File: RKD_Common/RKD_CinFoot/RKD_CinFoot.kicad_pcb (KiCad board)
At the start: 2 copper layers, 81 x 11.9 mm, 5 parts

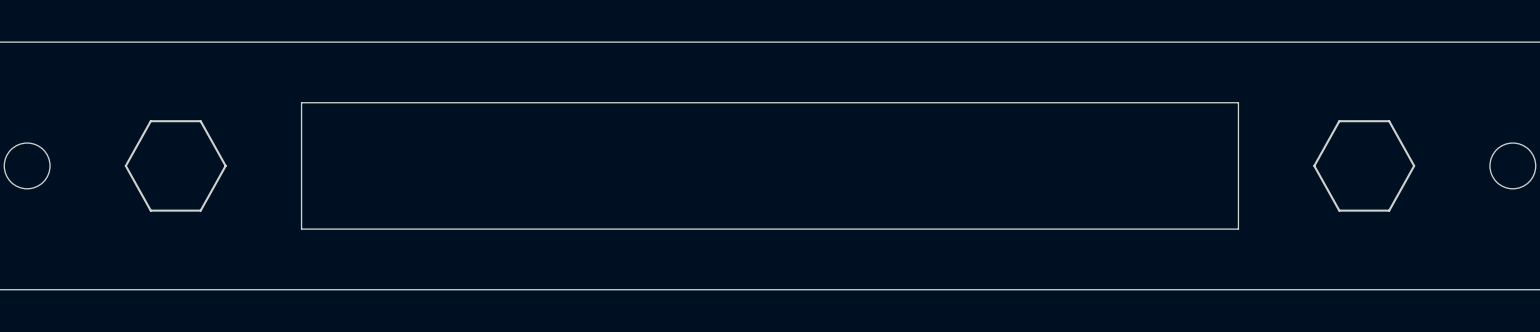
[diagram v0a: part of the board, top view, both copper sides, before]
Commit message: 部品誤り修正
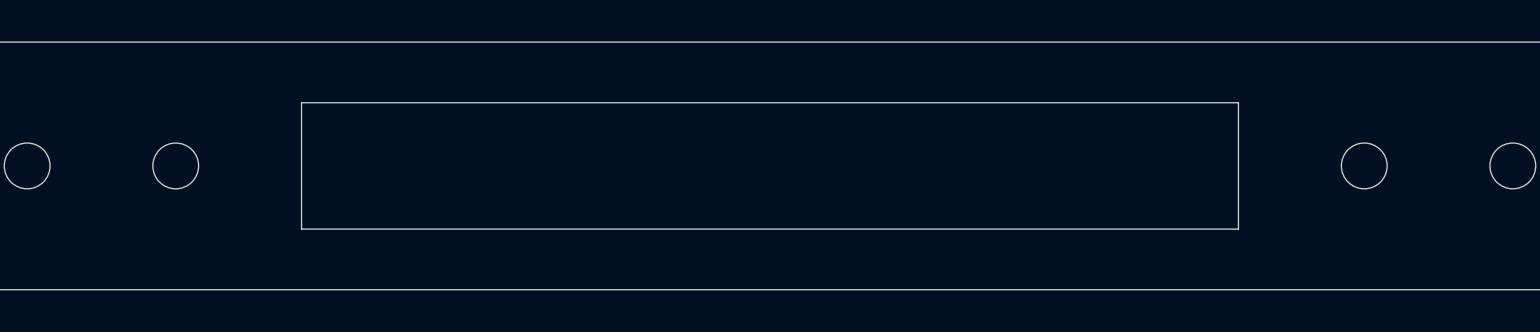
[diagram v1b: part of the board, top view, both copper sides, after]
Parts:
- Ref** (x2): footprint kbd_Hole:m2_Spacer_Hole_hex -> kbd_Hole:m2_Screw_Hole
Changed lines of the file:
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@@
 		)
 	)
-	(footprint "kbd_Hole:m2_Spacer_Hole_hex"
+	(footprint "kbd_Hole:m2_Screw_Hole"
 		(layer "F.Cu")
 		(at 121.44375 51.196875)
@@
 			)
 		)
-		(property "Footprint" "kbd_Hole:m2_Spacer_Hole_hex"
+		(property "Footprint" "kbd_Hole:m2_Screw_Hole"
 			(at 0 0 0)
 			(layer "F.Fab")
@@
 		)
 		(attr exclude_from_pos_files exclude_from_bom)
-		(fp_line
-			(start -2.4 0)
-			(end -1.2 2.15)
+		(fp_circle
+			(center 0 0)
+			(end 2.2 0)
 			(stroke
-				(width 0.1)
+				(width 0.15)
 				(type solid)
 			)
-			(layer "Edge.Cuts")
+			(fill none)
+			(layer "Cmts.User")
 		)
-		(fp_line
-			(start -1.2 -2.15)
-			(end -2.4 0)
+		(fp_circle
+			(center 0 0)
+			(end 2.45 0)
 			(stroke
-				(width 0.1)
+				(width 0.05)
 				(type solid)
 			)
-			(layer "Edge.Cuts")
+			(fill none)
+			(layer "F.CrtYd")
 		)
-		(fp_line
-			(start -1.2 2.15)
-			(end 1.2 2.15)
-			(stroke
-				(width 0.1)
-				(type solid)
+		(fp_text user "${REFERENCE}"
+			(at 0.3 0 0)
+			(layer "F.Fab")
+			(effects
+				(font
+					(size 1 1)
+					(thickness 0.15)
+				)
 			)
-			(layer "Edge.Cuts")
 		)
-		(fp_line
-			(start 1.2 -2.15)
-			(end -1.2 -2.15)
-			(stroke
-				(width 0.1)
-				(type solid)
-			)
-			(layer "Edge.Cuts")
-		)
-		(fp_line
-			(start 1.2 2.15)
-			(end 2.4 0)
-			(stroke
-				(width 0.1)
-				(type solid)
-			)
-			(layer "Edge.Cuts")
-		)
-		(fp_line
-			(start 2.4 0)
-			(end 1.2 -2.15)
-			(stroke
-				(width 0.1)
-				(type solid)
-			)
-			(layer "Edge.Cuts")
+		(pad "" np_thru_hole circle
+			(at 0 0)
+			(size 2.2 2.2)
+			(drill 2.2)
+			(layers "*.Cu" "*.Mask")
 		)
 	)
-	(footprint "kbd_Hole:m2_Spacer_Hole_hex"
+	(footprint "kbd_Hole:m2_Screw_Hole"
 		(layer "F.Cu")
 		(at 64.29375 51.196875)
@@
 			)
 		)
-		(property "Footprint" "kbd_Hole:m2_Spacer_Hole_hex"
+		(property "Footprint" "kbd_Hole:m2_Screw_Hole"
 			(at 0 0 0)
 			(layer "F.Fab")
@@
 		)
 		(attr exclude_from_pos_files exclude_from_bom)
-		(fp_line
-			(start -2.4 0)
-			(end -1.2 2.15)
+		(fp_circle
+			(center 0 0)
+			(end 2.2 0)
 			(stroke
-				(width 0.1)
+				(width 0.15)
 				(type solid)
 			)
-			(layer "Edge.Cuts")
+			(fill none)
+			(layer "Cmts.User")
 		)
-		(fp_line
-			(start -1.2 -2.15)
-			(end -2.4 0)
+		(fp_circle
+			(center 0 0)
+			(end 2.45 0)
 			(stroke
-				(width 0.1)
+				(width 0.05)
 				(type solid)
 			)
-			(layer "Edge.Cuts")
+			(fill none)
+			(layer "F.CrtYd")
 		)
-		(fp_line
-			(start -1.2 2.15)
-			(end 1.2 2.15)
-			(stroke
-				(width 0.1)
-				(type solid)
+		(fp_text user "${REFERENCE}"
+			(at 0.3 0 0)
+			(layer "F.Fab")
+			(effects
+				(font
+					(size 1 1)
+					(thickness 0.15)
+				)
 			)
-			(layer "Edge.Cuts")
 		)
-		(fp_line
-			(start 1.2 -2.15)
-			(end -1.2 -2.15)
-			(stroke
-				(width 0.1)
-				(type solid)
-			)
-			(layer "Edge.Cuts")
-		)
-		(fp_line
-			(start 1.2 2.15)
-			(end 2.4 0)
-			(stroke
-				(width 0.1)
-				(type solid)
-			)
-			(layer "Edge.Cuts")
-		)
-		(fp_line
-			(start 2.4 0)
-			(end 1.2 -2.15)
-			(stroke
-				(width 0.1)
-				(type solid)
-			)
-			(layer "Edge.Cuts")
+		(pad "" np_thru_hole circle
+			(at 0 0)
+			(size 2.2 2.2)
+			(drill 2.2)
+			(layers "*.Cu" "*.Mask")
 		)
 	)

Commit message: Common UpdateFootPrint
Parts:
- removed the Ref** at (128.6, 51.2)
- removed the Ref** at (121.4, 51.2)
- removed the Ref** at (64.3, 51.2)
- removed the Ref** at (57.1, 51.2)
- added Ref**: Val**, kbd_Hole:m2_Screw_Hole, F.Cu at (123.2, 67.0)
- added Ref**: Val**, kbd_Hole:m2_Screw_Hole, F.Cu at (58.9, 67.0)
- added Ref**: Val**, kbd_Hole:m2_Screw_Hole, F.Cu at (66.1, 67.0)
- added Ref**: Val**, kbd_Hole:m2_Screw_Hole, F.Cu at (130.4, 67.0)
- moved LED3 15.9 mm to (94.7, 67.0)
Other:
- board size 81 x 11.9 mm -> 76.2 x 11.9 mm
- board text added: "RKD_CinderellaFoot v1.0"
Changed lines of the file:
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@@
 	(footprint "kbd_Hole:m2_Screw_Hole"
 		(layer "F.Cu")
-		(at 128.5875 51.196875)
+		(at 123.229892 66.972702)
 		(descr "Mounting Hole 2.2mm, no annular, M2")
 		(tags "mounting hole 2.2mm no annular m2")
@@
 	(footprint "kbd_Hole:m2_Screw_Hole"
 		(layer "F.Cu")
-		(at 121.44375 51.196875)
+		(at 58.936142 66.972702)
 		(descr "Mounting Hole 2.2mm, no annular, M2")
 		(tags "mounting hole 2.2mm no annular m2")
@@
 	(footprint "kbd_Hole:m2_Screw_Hole"
 		(layer "F.Cu")
-		(at 64.29375 51.196875)
+		(at 66.079892 66.972702)
 		(descr "Mounting Hole 2.2mm, no annular, M2")
 		(tags "mounting hole 2.2mm no annular m2")
@@
 		)
 	)
+	(footprint "Rikkodo_FootPrint:rkd_KeyHall_6wx45_Cinderella"
+		(layer "F.Cu")
+		(at 94.654952 66.972702)
+		(property "Reference" "LED3"
+			(at 6 0.5 0)
+			(layer "F.SilkS")
+			(hide yes)
+			(effects
+				(font
+					(size 1 1)
+					(thickness 0.15)
+				)
+			)
+		)
+		(property "Value" "LED_SK6812MINI-E"
+			(at -5.5 -0.5 0)
+			(layer "F.Fab")
+			(hide yes)
+			(effects
+				(font
+					(size 1 1)
+					(thickness 0.15)
+				)
+			)
+		)
+		(property "Footprint" "Rikkodo_FootPrint:rkd_KeyHall_6wx45_Cinderella"
+			(at 0 0 0)
+			(layer "F.Fab")
+			(hide yes)
+			(effects
+				(font
+					(size 1.27 1.27)
+					(thickness 0.15)
+				)
+			)
+		)
+		(property "Datasheet" ""
+			(at 0 0 0)
+			(layer "F.Fab")
+			(hide yes)
+			(effects
+				(font
+					(size 1.27 1.27)
+					(thickness 0.15)
+				)
+			)
+		)
+		(property "Description" ""
+			(at 0 0 0)
+			(layer "F.Fab")
+			(hide yes)
+			(effects
+				(font
+					(size 1.27 1.27)
+					(thickness 0.15)
+				)
+			)
+		)
+		(attr through_hole)
+		(fp_line
+			(start -22.775 3.3875)
+			(end -22.775 -3.3875)
+			(stroke
+				(width 0.05)
+				(type default)
+			)
+			(layer "Edge.Cuts")
+		)
+		(fp_line
+			(start 22.775 -3.3875)
+			(end -22.775 -3.3875)
+			(stroke
+				(width 0.05)
+				(type default)
+			)
+			(layer "Edge.Cuts")
+		)
+		(fp_line
+			(start 22.775 -3.3875)
+			(end 22.775 3.3875)
+			(stroke
+				(width 0.05)
+				(type default)
+			)
+			(layer "Edge.Cuts")
+		)
+		(fp_line
+			(start 22.775 3.3875)
+			(end -22.775 3.3875)
+			(stroke
+				(width 0.05)
+				(type default)
+			)
+			(layer "Edge.Cuts")
+		)
+	)
 	(footprint "kbd_Hole:m2_Screw_Hole"
 		(layer "F.Cu")
-		(at 57.15 51.196875)
+		(at 130.373642 66.972702)
 		(descr "Mounting Hole 2.2mm, no annular, M2")
 		(tags "mounting hole 2.2mm no annular m2")
@@
 		)
 	)
-	(footprint "Rikkodo_FootPrint:rkd_KeyHall_6wx45_Cinderella"
-		(layer "F.Cu")
-		(at 92.86875 51.196875)
-		(property "Reference" "LED3"
-			(at 6 0.5 0)
-			(layer "F.SilkS")
-			(hide yes)
-			(effects
-				(font
-					(size 1 1)
-					(thickness 0.15)
-				)
-			)
-		)
-		(property "Value" "LED_SK6812MINI-E"
-			(at -5.5 -0.5 0)
-			(layer "F.Fab")
-			(hide yes)
-			(effects
-				(font
-					(size 1 1)
-					(thickness 0.15)
-				)
-			)
-		)
-		(property "Footprint" "Rikkodo_FootPrint:rkd_KeyHall_6wx45_Cinderella"
-			(at 0 0 0)
-			(layer "F.Fab")
-			(hide yes)
-			(effects
-				(font
-					(size 1.27 1.27)
-					(thickness 0.15)
-				)
-			)
-		)
-		(property "Datasheet" ""
-			(at 0 0 0)
-			(layer "F.Fab")
-			(hide yes)
-			(effects
-				(font
-					(size 1.27 1.27)
-					(thickness 0.15)
-				)
-			)
-		)
-		(property "Description" ""
-			(at 0 0 0)
-			(layer "F.Fab")
-			(hide yes)
-			(effects
-				(font
-					(size 1.27 1.27)
-					(thickness 0.15)
-				)
-			)
-		)
-		(attr through_hole)
-		(fp_line
-			(start -22.525 3.0375)
-			(end -22.525 -3.0375)
-			(stroke
-				(width 0.05)
-				(type default)
-			)
-			(layer "Edge.Cuts")
-		)
-		(fp_line
-			(start 22.525 -3.0375)
-			(end -22.525 -3.0375)
-			(stroke
-				(width 0.05)
-				(type default)
-			)
-			(layer "Edge.Cuts")
-		)
-		(fp_line
-			(start 22.525 -3.0375)
-			(end 22.525 3.0375)
-			(stroke
-				(width 0.05)
-				(type default)
-			)
-			(layer "Edge.Cuts")
-		)
-		(fp_line
-			(start 22.525 3.0375)
-			(end -22.525 3.0375)
-			(stroke
-				(width 0.05)
-				(type default)
-			)
-			(layer "Edge.Cuts")
-		)
-	)
 	(gr_arc
-		(start 133.35 55.959375)
-		(mid 133.001274 56.801274)
-		(end 132.159375 57.15)
-		(stroke
-			(width 0.05)
-			(type default)
-		)
-		(layer "Edge.Cuts")
-	)
-	(gr_line
-		(start 132.159375 45.24375)
-		(end 53.578125 45.24375)
+		(start 56.554801 62.210138)
+		(mid 56.903527 61.368239)
+		(end 57.745426 61.019513)
 		(stroke
 			(width 0.05)
@@
 	)
 	(gr_arc
-		(start 52.3875 46.434375)
-		(mid 52.736226 45.592476)
-		(end 53.578125 45.24375)
-		(stroke
-			(width 0.05)
-			(type default)
-		)
-		(layer "Edge.Cuts")
-	)
-	(gr_line
-		(start 132.159375 57.15)
-		(end 53.578125 57.15)
-		(stroke
-			(width 0.05)
-			(type default)
-		)
-		(layer "Edge.Cuts")
-	)
-	(gr_line
-		(start 52.3875 46.434375)
-		(end 52.3875 55.959375)
+		(start 131.564299 61.019573)
+		(mid 132.406196 61.368303)
+		(end 132.754924 62.210198)
 		(stroke
 			(width 0.05)
@@
 	)
 	(gr_arc
-		(start 53.578125 57.15)
-		(mid 52.736226 56.801274)
-		(end 52.3875 55.959375)
+		(start 132.754898 71.7351)
+		(mid 132.406149 72.576979)
+		(end 131.564273 72.925725)
+		(stroke
+			(width 0.05)
+			(type default)
+		)
+		(layer "Edge.Cuts")
+	)
+	(gr_line
+		(start 56.55486 62.210206)
+		(end 56.55486 71.735206)
+		(stroke
+			(width 0.05)
+			(type default)
+		)
+		(layer "Edge.Cuts")
+	)
+	(gr_line
+		(start 131.564299 61.019573)
+		(end 57.745486 61.019572)
+		(stroke
+			(width 0.05)
+			(type default)
+		)
+		(layer "Edge.Cuts")
+	)
+	(gr_line
+		(start 113.109506 72.92572)
+		(end 76.199936 72.92572)
+		(stroke
+			(width 0.05)
+			(type default)
+		)
+		(layer "Edge.Cuts")
+	)
+	(gr_line
+		(start 132.754924 62.210202)
+		(end 132.754924 71.735202)
+		(stroke
+			(width 0.05)
+			(type default)
+		)
+		(layer "Edge.Cuts")
+	)
+	(gr_line
+		(start 73.818684 72.92572)
+		(end 76.199936 72.92572)
+		(stroke
+			(width 0.05)
+			(type default)
+		)
+		(layer "Edge.Cuts")
+	)
+	(gr_line
+		(start 131.564273 72.925725)
+		(end 115.490758 72.92572)
+		(stroke
+			(width 0.05)
+			(type default)
+		)
+		(layer "Edge.Cuts")
+	)
+	(gr_line
+		(start 73.818684 72.92572)
+		(end 57.74551 72.925882)
+		(stroke
+			(width 0.05)
+			(type default)
+		)
+		(layer "Edge.Cuts")
+	)
+	(gr_line
+		(start 113.109506 72.92572)
+		(end 115.490758 72.92572)
 		(stroke
 			(width 0.05)
@@
 	)
 	(gr_arc
-		(start 132.159375 45.24375)
-		(mid 133.001274 45.592476)
-		(end 133.35 46.434375)
-		(stroke
-			(width 0.05)
-			(type default)
-		)
-		(layer "Edge.Cuts")
-	)
-	(gr_line
-		(start 133.35 46.434375)
-		(end 133.35 55.959375)
-		(stroke
-			(width 0.05)
-			(type default)
-		)
-		(layer "Edge.Cuts")
+		(start 57.74551 72.925882)
+		(mid 56.903619 72.577148)
+		(end 56.554885 71.735257)
+		(stroke
+			(width 0.05)
+			(type default)
+		)
+		(layer "Edge.Cuts")
+	)
+	(gr_text "RKD_CinderellaFoot v1.0"
+		(at 126.801768 63.400776 0)
+		(layer "B.SilkS")
+		(effects
+			(font
+				(size 1 1)
+				(thickness 0.1)
+			)
+			(justify left bottom mirror)
+		)
+	)
+	(group ""
+		(members "119e2f71-e038-4129-bcec-3b2945375254" "12d03c72-44ba-4fbf-9bdb-823f6eced25d"
+			"16bad5ad-64f4-4ff5-9c23-298ea4e017e0" "2d08a7a3-aff4-414f-80d4-dfe93a1a73b3"
+			"4b89dfa1-3103-4fc7-b920-419c784dca03" "5400b3c1-3551-4653-a554-9fc24ae7e6c9"
+			"58eba527-2dd0-4d75-a348-94fd6b5970e9" "6916fafc-4c17-4f8d-bbd2-5a074d22d2be"
+			"9630daa5-5a4f-4a8d-a5d8-1ed182757a9f" "a1a3cc95-14b8-4f0b-8d59-1c5646ffd4df"
+			"ad41452a-3768-487e-8399-df2d8a481663" "cc8f9f2b-929e-4d7d-af00-9575b9b466ea"
+			"ce852a84-7158-4034-ae7a-1c5c82d03b17" "d2d7e6a8-f0bb-4800-bf21-3aaf7924e472"
+			"ddc9a58e-fcee-494e-bcdc-0e873c863eda" "e78b853e-3f1f-40d2-b961-3e6054a4ac34"
+			"ecdd45a8-3b2b-41a6-be5a-94f1dfb6cd63" "fe343bde-19ee-4b08-a2df-0cf6b1d1d7c2"
+		)
 	)
 )
